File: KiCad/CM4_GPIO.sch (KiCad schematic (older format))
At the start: 16 parts, among them J16 GSD090012SEU, J17 Conn_02x04_Odd_Even, J18 ARJM11C7-502-AB-ER2-T, J19 Conn_02x20_Odd_Even, J20 Conn_02x04_Odd_Even, U6 74LVC1G07GW, U7 TPD4EUSB30, U8 RT9742GGJ5, U9 TPD4EUSB30

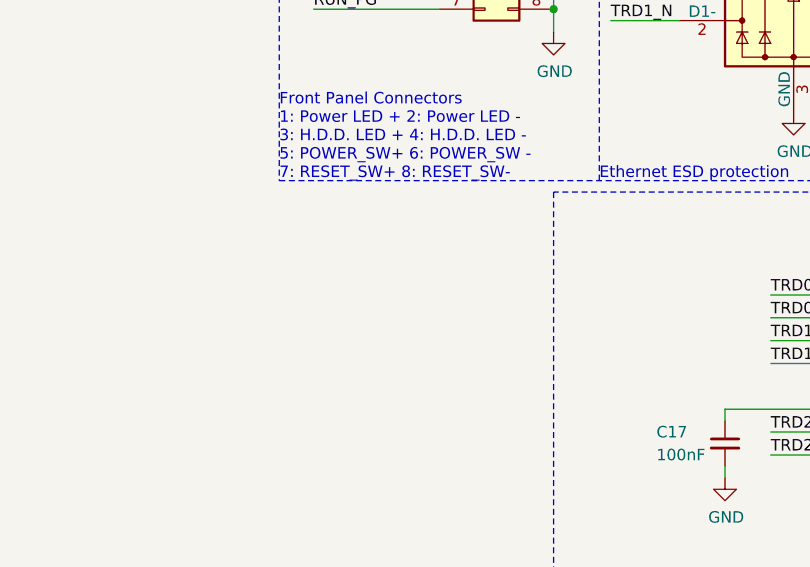
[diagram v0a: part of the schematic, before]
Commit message: added jumper for GPIO_VREF selection
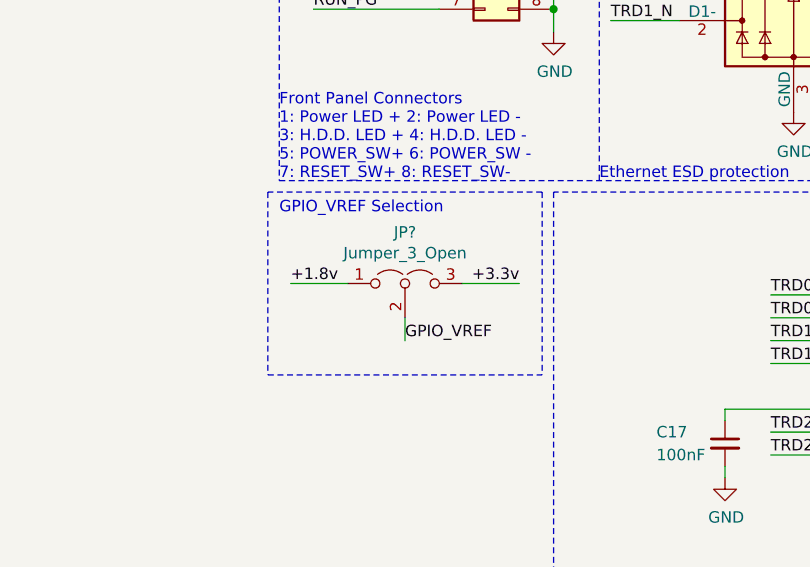
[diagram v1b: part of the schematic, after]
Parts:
- added JP?: Jumper_3_Open, CM4_MATX:PinHeader_1x03_P2.54mm_Vertical, symbol CM4_MATX:Jumper_3_Open
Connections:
- net +1.8v: now also JP?.1 (A)
- net +3.3v: now also JP?.3 (B)
- net GPIO_VREF: now also JP?.2 (C)
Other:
- note added: "GPIO_VREF Selection"
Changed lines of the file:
@@
 Wire Wire Line
 	8350 5650 8350 5700
+$Comp
+L CM4_MATX:Jumper_3_Open JP?
+U 1 1 602A5D6A
+P 6950 4850
+F 0 "JP?" H 6950 5074 50  0000 C CNN
+F 1 "Jumper_3_Open" H 6950 4983 50  0000 C CNN
+F 2 "CM4_MATX:PinHeader_1x03_P2.54mm_Vertical" H 6950 4850 50  0001 C CNN
+F 3 "~" H 6950 4850 50  0001 C CNN
+	1    6950 4850
+	1    0    0    -1
+$EndComp
+Wire Wire Line
+	7200 4850 7450 4850
+Wire Wire Line
+	6450 4850 6700 4850
+Text Label 6950 5100 0    50   ~ 0
+GPIO_VREF
+Wire Wire Line
+	6950 5000 6950 5100
+Text Label 6450 4850 0    50   ~ 0
++1.8v
+Text Label 7450 4850 2    50   ~ 0
++3.3v
+Wire Notes Line
+	7550 4450 6350 4450
+Wire Notes Line
+	6350 5250 7550 5250
+Text Notes 6400 4550 0    50   ~ 0
+GPIO_VREF Selection
+Wire Notes Line
+	7550 4450 7550 5250
+Wire Notes Line
+	6350 4450 6350 5250
 $EndSCHEMATC

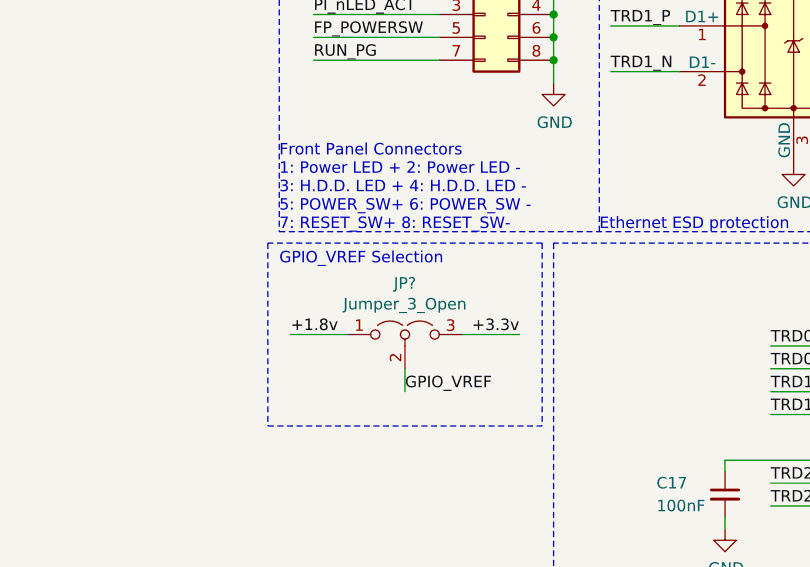
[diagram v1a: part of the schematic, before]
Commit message: updated part numerations
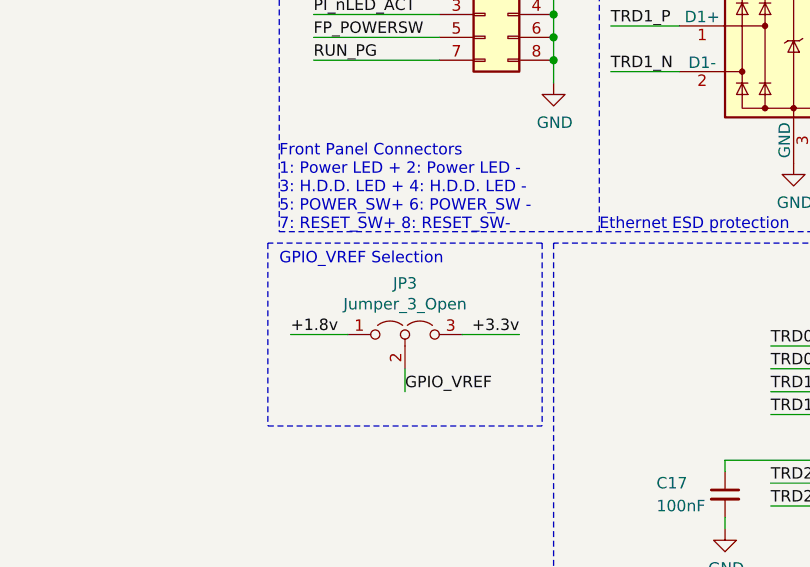
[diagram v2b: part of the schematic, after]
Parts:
- gave numbers to parts that had none: 1
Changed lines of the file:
@@
 	8350 5650 8350 5700
 $Comp
-L CM4_MATX:Jumper_3_Open JP?
+L CM4_MATX:Jumper_3_Open JP3
 U 1 1 602A5D6A
 P 6950 4850
-F 0 "JP?" H 6950 5074 50  0000 C CNN
+F 0 "JP3" H 6950 5074 50  0000 C CNN
 F 1 "Jumper_3_Open" H 6950 4983 50  0000 C CNN
 F 2 "CM4_MATX:PinHeader_1x03_P2.54mm_Vertical" H 6950 4850 50  0001 C CNN
